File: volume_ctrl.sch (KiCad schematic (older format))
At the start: 0 parts

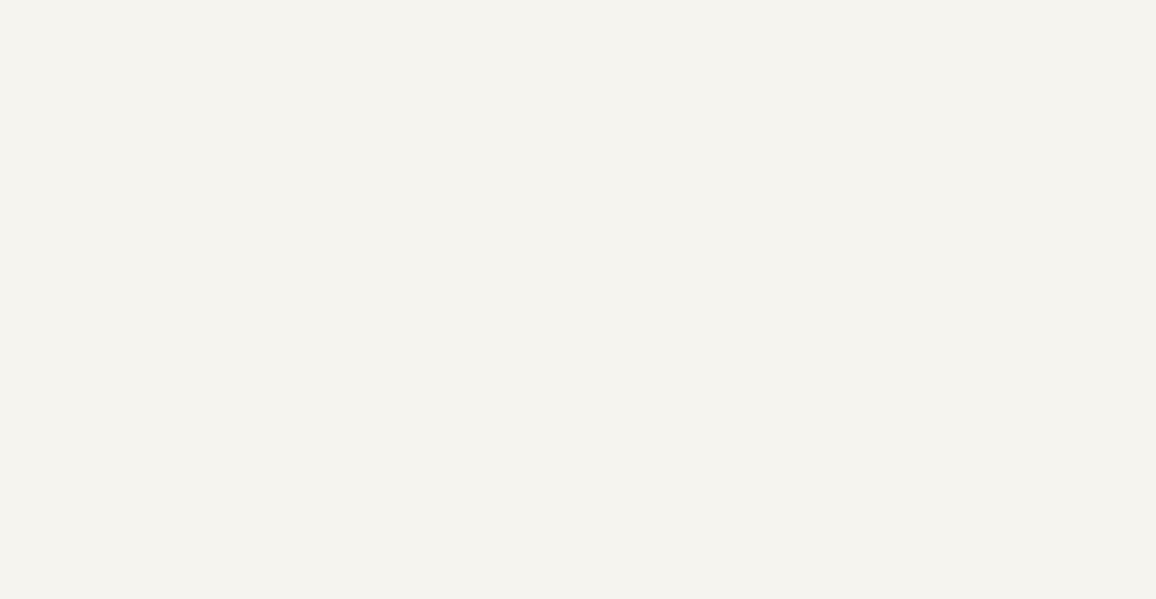
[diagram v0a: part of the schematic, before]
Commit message: Began placing volume circuit parts, placed a trim pot for R17 to allow pre-amp level adjustment.
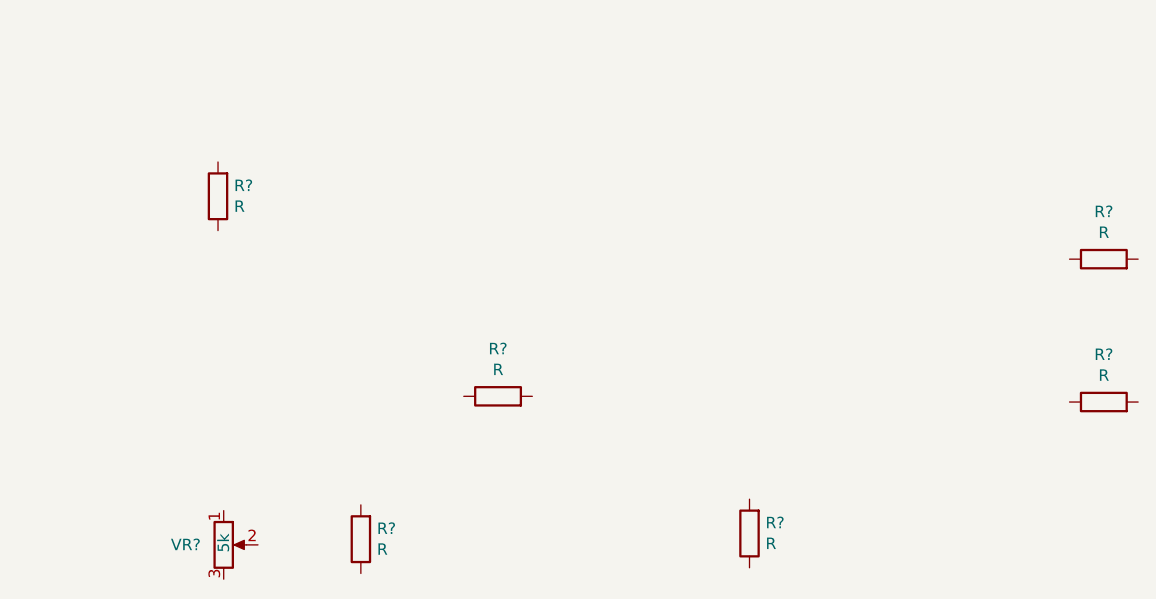
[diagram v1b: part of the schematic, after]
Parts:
- added R? (x6): R, symbol Device:R
- added VR?: 5k, Murata-POT:PV36W202C01B00, symbol Device:R_POT
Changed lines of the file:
@@
 Text HLabel 1250 1500 0    50   UnSpc ~ 0
 pot_3
+$Comp
+L Device:R_POT VR?
+U 1 1 5E268D61
+P 3275 4300
+AR Path="/5C7F608F/5E268D61" Ref="VR?"  Part="1"
+AR Path="/5E227FCE/5E268D61" Ref="VR?"  Part="1"
+F 0 "VR?" H 3175 4300 50  0000 R CNN
+F 1 "5k" V 3275 4350 50  0000 R CNN
+F 2 "Murata-POT:PV36W202C01B00" H 3275 4300 50  0001 C CNN
+F 3 "https://www.mouser.com/ProductDetail/Bourns/PV36W502C01B00?qs=BqPwLKJeIrffwfpi4cR%2Fyg%3D%3D&gclid=Cj0KCQiAvJXxBRCeARIsAMSkAprVNxrqciw2F2bbLEol0MFfB_kQMYkrvleaPlVNZV5jLL3ntUG4zu0aApSuEALw_wcB" H 3275 4300 50  0001 C CNN
+	1    3275 4300
+	1    0    0    -1
+$EndComp
+$Comp
+L Device:R R?
+U 1 1 5E26A320
+P 3875 4275
+F 0 "R?" H 3805 4229 50  0000 R CNN
+F 1 "R" H 3805 4320 50  0000 R CNN
+F 2 "" V 3805 4275 50  0001 C CNN
+F 3 "~" H 3875 4275 50  0001 C CNN
+	1    3875 4275
+	-1   0    0    1
+$EndComp
+$Comp
+L Device:R R?
+U 1 1 5E26AC16
+P 4475 3650
+F 0 "R?" V 4682 3650 50  0000 C CNN
+F 1 "R" V 4591 3650 50  0000 C CNN
+F 2 "" V 4405 3650 50  0001 C CNN
+F 3 "~" H 4475 3650 50  0001 C CNN
+	1    4475 3650
+	0    -1   -1   0
+$EndComp
+$Comp
+L Device:R R?
+U 1 1 5E26BC9E
+P 3250 2775
+F 0 "R?" H 3180 2729 50  0000 R CNN
+F 1 "R" H 3180 2820 50  0000 R CNN
+F 2 "" V 3180 2775 50  0001 C CNN
+F 3 "~" H 3250 2775 50  0001 C CNN
+	1    3250 2775
+	-1   0    0    1
+$EndComp
+$Comp
+L Device:R R?
+U 1 1 5E26C36A
+P 5575 4250
+F 0 "R?" H 5505 4204 50  0000 R CNN
+F 1 "R" H 5505 4295 50  0000 R CNN
+F 2 "" V 5505 4250 50  0001 C CNN
+F 3 "~" H 5575 4250 50  0001 C CNN
+	1    5575 4250
+	-1   0    0    1
+$EndComp
+$Comp
+L Device:R R?
+U 1 1 5E26C6A9
+P 7125 3675
+F 0 "R?" V 7332 3675 50  0000 C CNN
+F 1 "R" V 7241 3675 50  0000 C CNN
+F 2 "" V 7055 3675 50  0001 C CNN
+F 3 "~" H 7125 3675 50  0001 C CNN
+	1    7125 3675
+	0    -1   -1   0
+$EndComp
+$Comp
+L Device:R R?
+U 1 1 5E26CC02
+P 7125 3050
+F 0 "R?" V 7332 3050 50  0000 C CNN
+F 1 "R" V 7241 3050 50  0000 C CNN
+F 2 "" V 7055 3050 50  0001 C CNN
+F 3 "~" H 7125 3050 50  0001 C CNN
+	1    7125 3050
+	0    -1   -1   0
+$EndComp
 $EndSCHEMATC

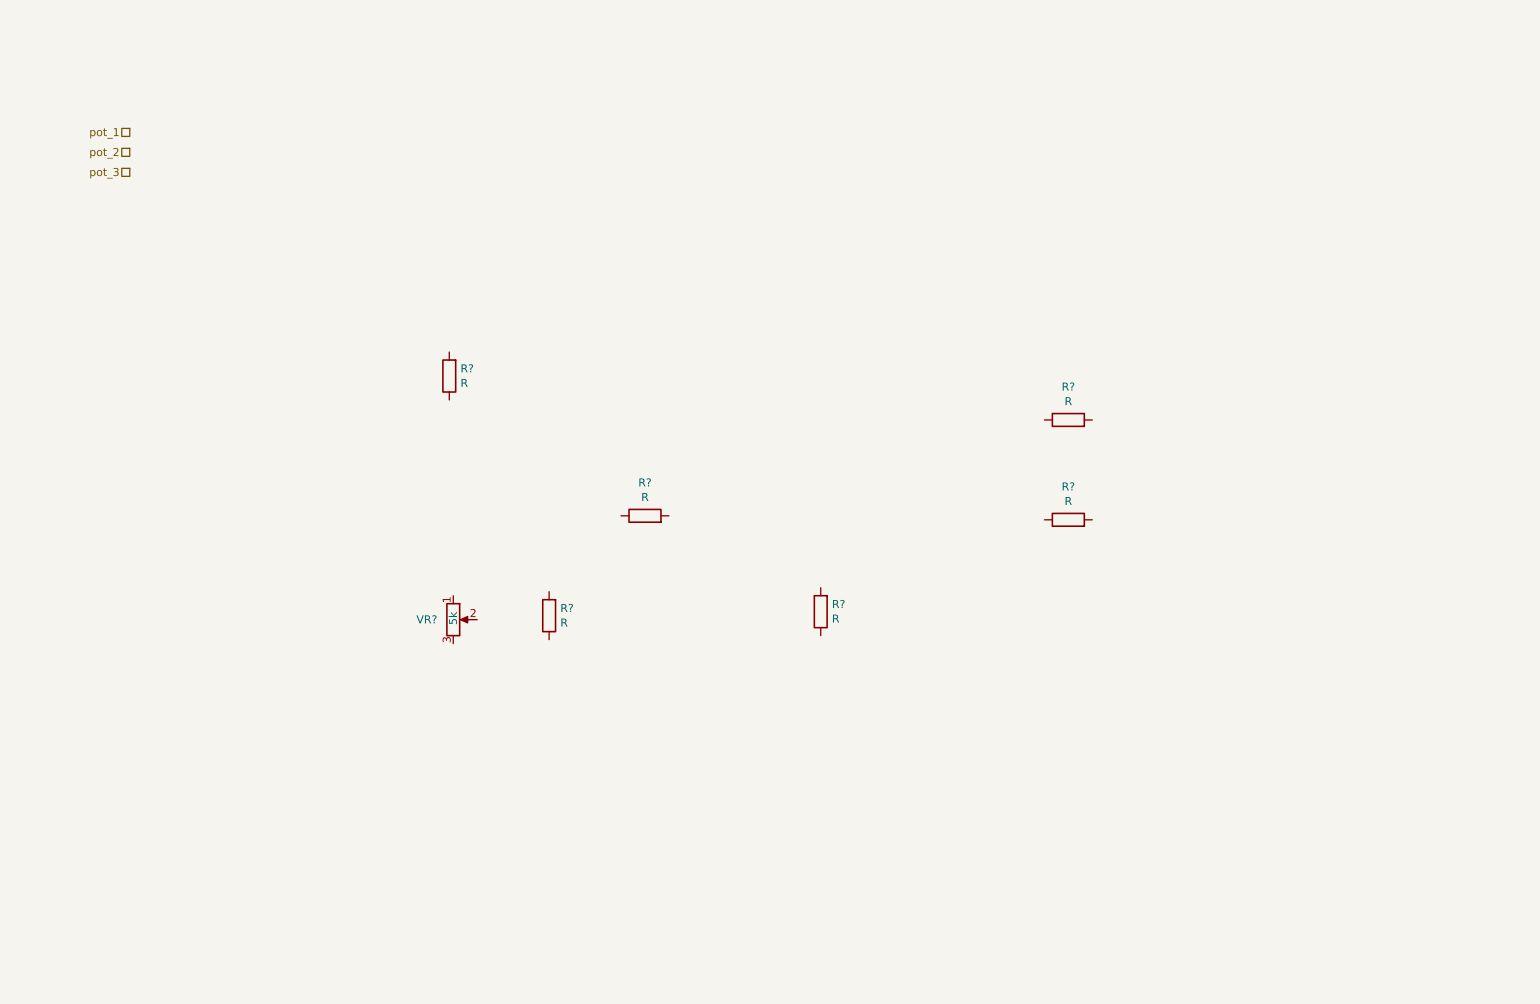
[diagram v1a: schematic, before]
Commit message: Volume circuit placed and connected. Page titles added.
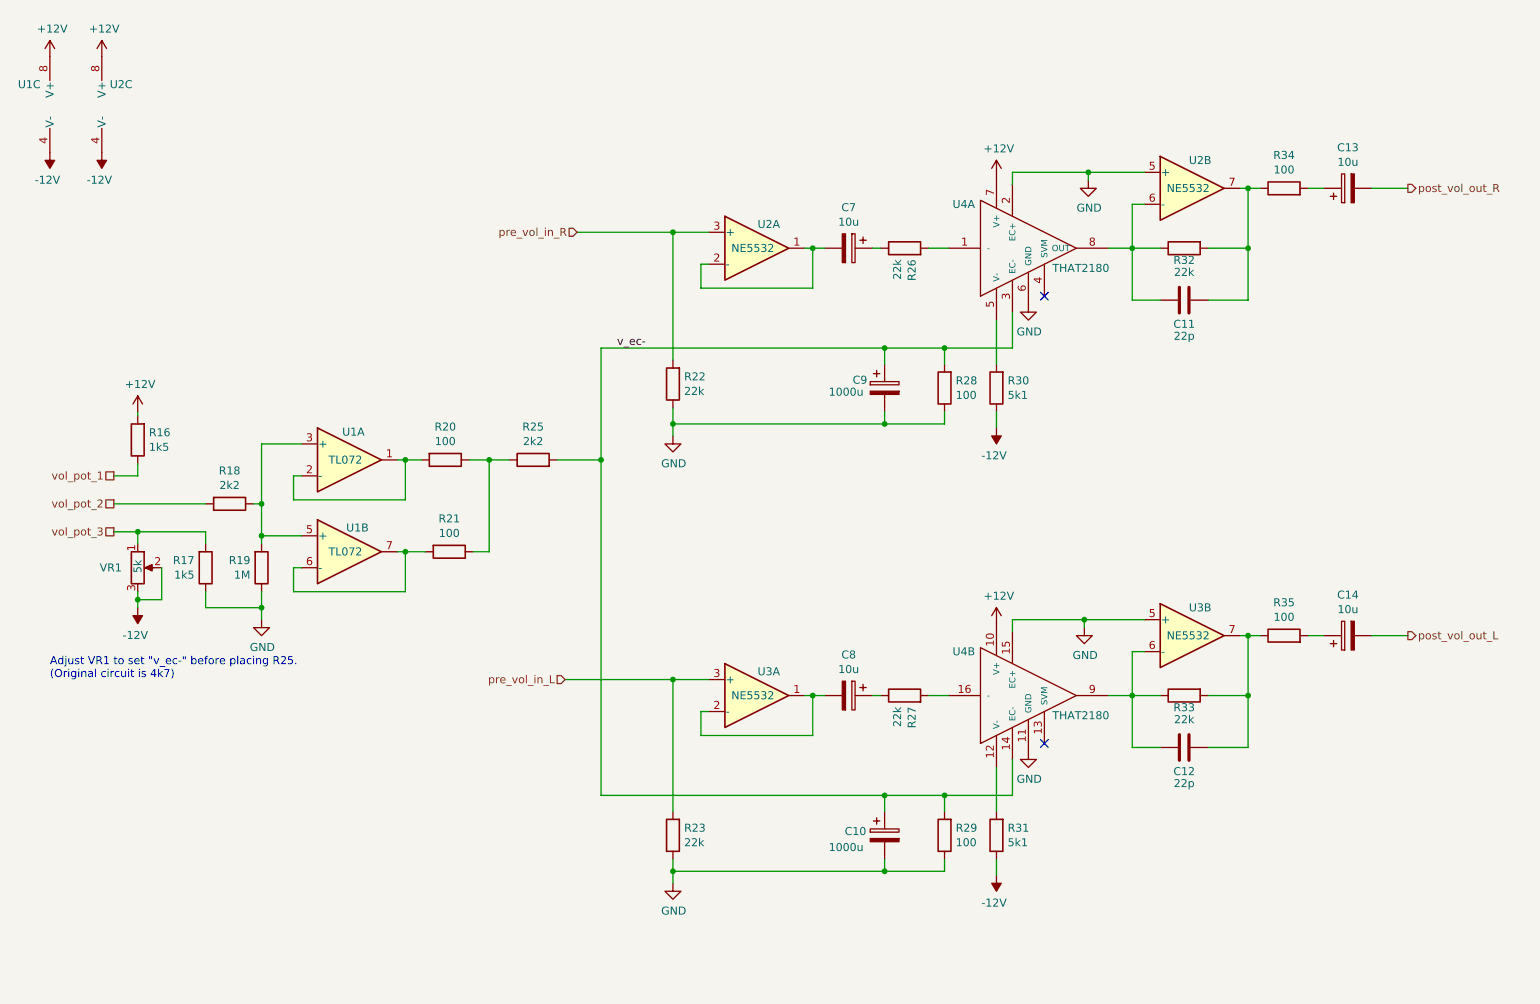
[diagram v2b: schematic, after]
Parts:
- added C10, C9: 1000u, symbol Device:CP
- added C11, C12: 22p, symbol Device:C
- added C13, C14, C7, C8: 10u, symbol Device:CP
- added R16, R17: 1k5, symbol Device:R
- added R18: 2k2, symbol Device:R
- added R19: 1M, symbol Device:R
- added R20, R21, R28, R29, R34: 100, symbol Device:R
- added R22, R26, R32: 22k, symbol Device:R
- added R30: 5k1, symbol Device:R
- added U1: TL072, Package_SO:SOIC-8_3.9x4.9mm_P1.27mm, symbol ne5532dr:TL072
- added U2, U3: NE5532, Package_SO:SOIC-8_3.9x4.9mm_P1.27mm, symbol Amplifier_Operational:NE5532
- added U4: THAT2180, Package_DIP:DIP-16_W7.62mm_SMDSocket_SmallPads, symbol audio_amp_custom:THAT2180
- R23, R27, R33: renamed from R?; value R -> 22k
- R25: renamed from R?; value R -> 2k2
- R31: renamed from R?; value R -> 5k1
- R35: renamed from R?; value R -> 100
- gave numbers to parts that had none: 1
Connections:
- net vol_pot_3: now reaches VR1.1
- net vol_pot_3: now also R17.2
- net -12V: now reaches VR1.2
- net -12V: now also R31.1, VR1.3, R30.1, U1.4 (V-), U2.4 (V-)
- net at R27.1: now also C8.1
- net at R27.2: now also U4.16 (-)
- net at R25.1: now also R20.1, R21.1
- net v_ec-: now reaches R25.2
- net v_ec-: now also C10.1, C9.1, R28.2, R29.2, U4.14 (EC-), U4.3 (EC-)
- net GND: now reaches R23.1
- net GND: now also C10.2, C9.2, R17.1, R19.1, R22.1, R28.1, R29.1, U2.5 (+), U3.5 (+), U4.11 (GND), U4.15 (EC+), U4.2 (EC+), U4.6 (GND)
- net pre_vol_in_L: now reaches R23.2
- net pre_vol_in_L: now also U3.3 (+)
- net at R31.2: now also U4.12 (V-)
- net at R35.1: now also R33.2, C12.1, U3.7
- net at R35.2: now also C14.1
- net at R33.1: now also C12.2, U3.6 (-), U4.9
- new net: R26.2, U4.1 (-)
- new net: R30.2, U4.5 (V-)
- new net: C11.2, R32.1, U2.6 (-), U4.8 (OUT)
- new net: C8.2, U3.1, U3.2 (-)
- new net: R20.2, U1.1, U1.2 (-)
- new net: R21.2, U1.6 (-), U1.7
- new net: R18.1, R19.2, U1.3 (+), U1.5 (+)
- new net: C7.1, R26.1
- new net: C11.1, R32.2, R34.1, U2.7
- new net: C13.1, R34.2
- new net: C7.2, U2.1, U2.2 (-)
- new net +12V: R16.2, U1.8 (V+), U2.8 (V+), U4.10 (V+), U4.7 (V+)
- new net post_vol_out_L: C14.2
- new net post_vol_out_R: C13.2
- new net pre_vol_in_R: R22.2, U2.3 (+)
- new net vol_pot_1: R16.1
- new net vol_pot_2: R18.2
- no-connect marks 0 -> 2
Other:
- note added: "Adjust VR1 to set "v_ec-" before placing R25.\n(Original circuit is 4k7)"
- moved on the sheet: R23, R25, R27, R31, R33, R35, VR1

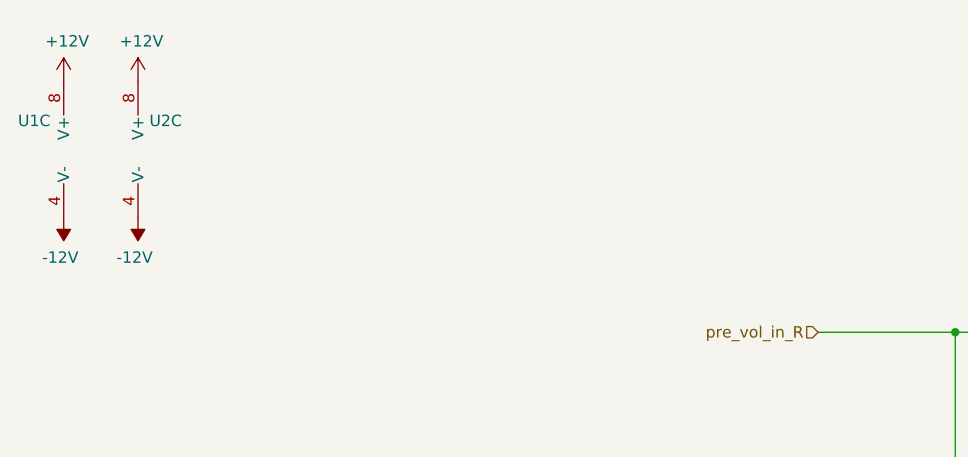
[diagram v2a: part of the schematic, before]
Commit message: Started input select circuit.
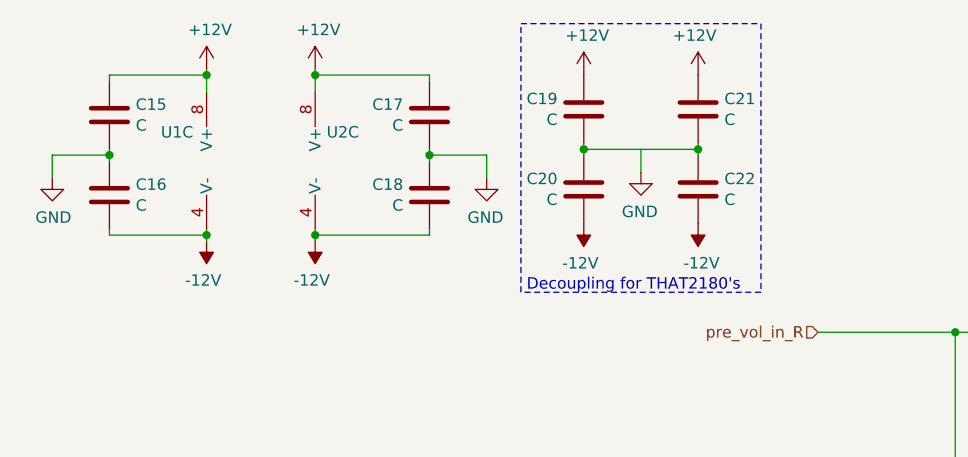
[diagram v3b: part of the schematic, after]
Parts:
- added C15, C16, C17, C18, C19, C20, C21, C22: C, symbol Device:C
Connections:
- net +12V: now also C15.1, C17.1, C19.1, C21.1
- net -12V: now also C16.2, C18.2, C20.2, C22.2
- net GND: now also C15.2, C16.1, C17.2, C18.1, C19.2, C20.1, C21.2, C22.1
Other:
- note added: "Decoupling for THAT2180's"
- moved on the sheet: U1C, U2C

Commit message: Opened on home office computer. Some rescue and lib conversion happened. Need to confirm no changes on work laptop.
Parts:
- U1: symbol ne5532dr:TL072 -> AAMB-rescue:TL072-ne5532dr
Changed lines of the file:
@@
 EESchema Schematic File Version 4
-LIBS:AAMB-cache
 EELAYER 30 0
 EELAYER END
@@
 $EndComp
 $Comp
-L ne5532dr:TL072 U1
+L AAMB-rescue:TL072-ne5532dr U1
 U 1 1 5E2ABF79
 P 2625 3300
@@
 $EndComp
 $Comp
-L ne5532dr:TL072 U1
+L AAMB-rescue:TL072-ne5532dr U1
 U 2 1 5E2B056B
 P 2625 3875
@@
 $EndComp
 $Comp
-L ne5532dr:TL072 U1
+L AAMB-rescue:TL072-ne5532dr U1
 U 3 1 5E2B20B5
 P 1475 1125
